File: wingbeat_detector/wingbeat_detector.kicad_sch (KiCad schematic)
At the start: 9 parts, among them J1 USB_C_10137062-00021LF, J2 CONN_UMC_JACK_SMD, U1 UAF42_SMA, U2 MAX865EUA+

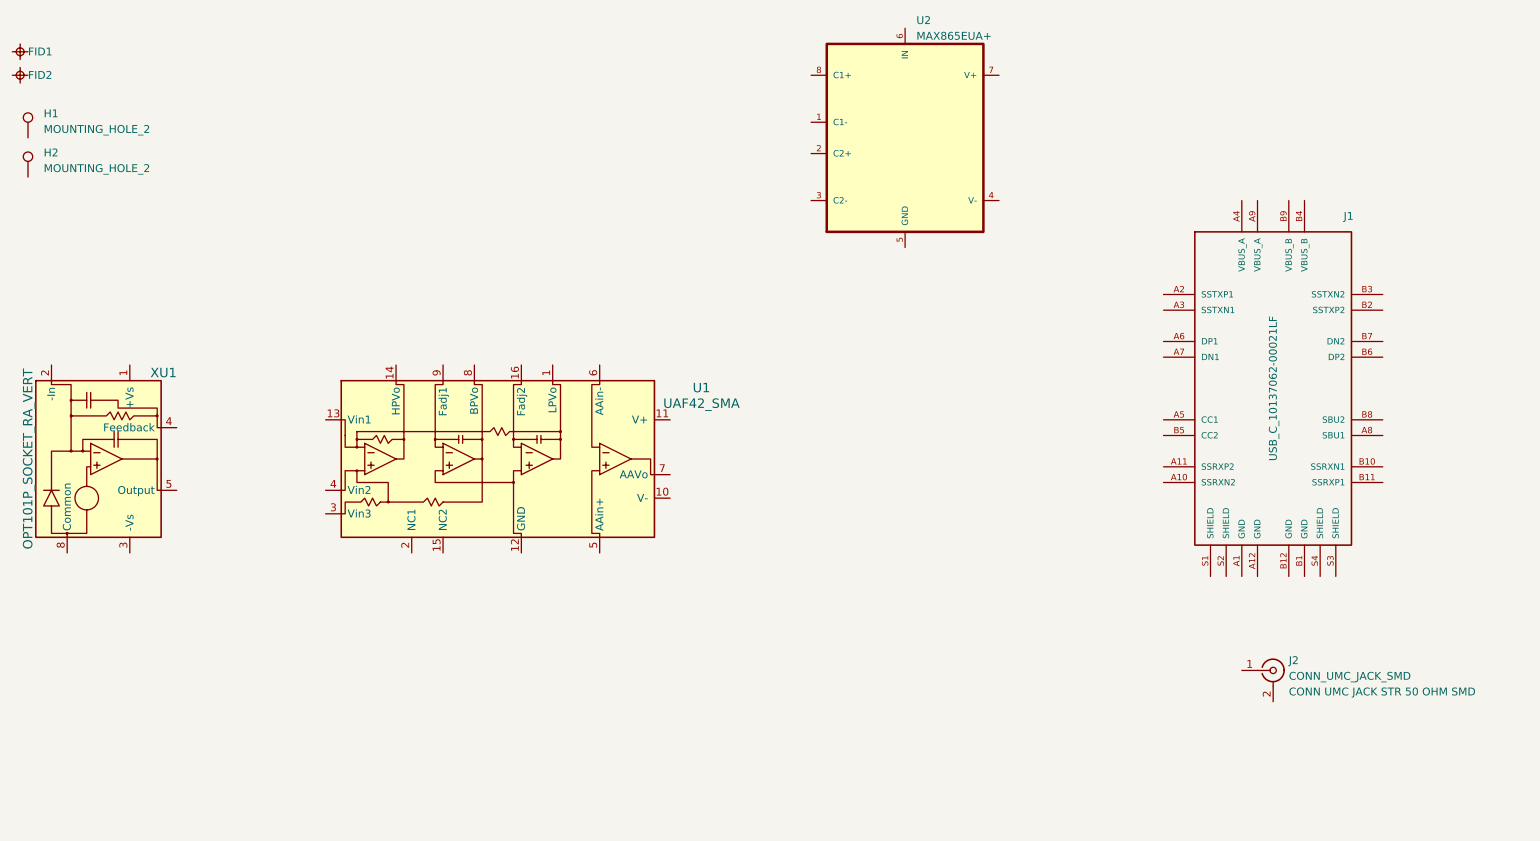
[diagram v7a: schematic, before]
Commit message: Remove OPT101 and replace
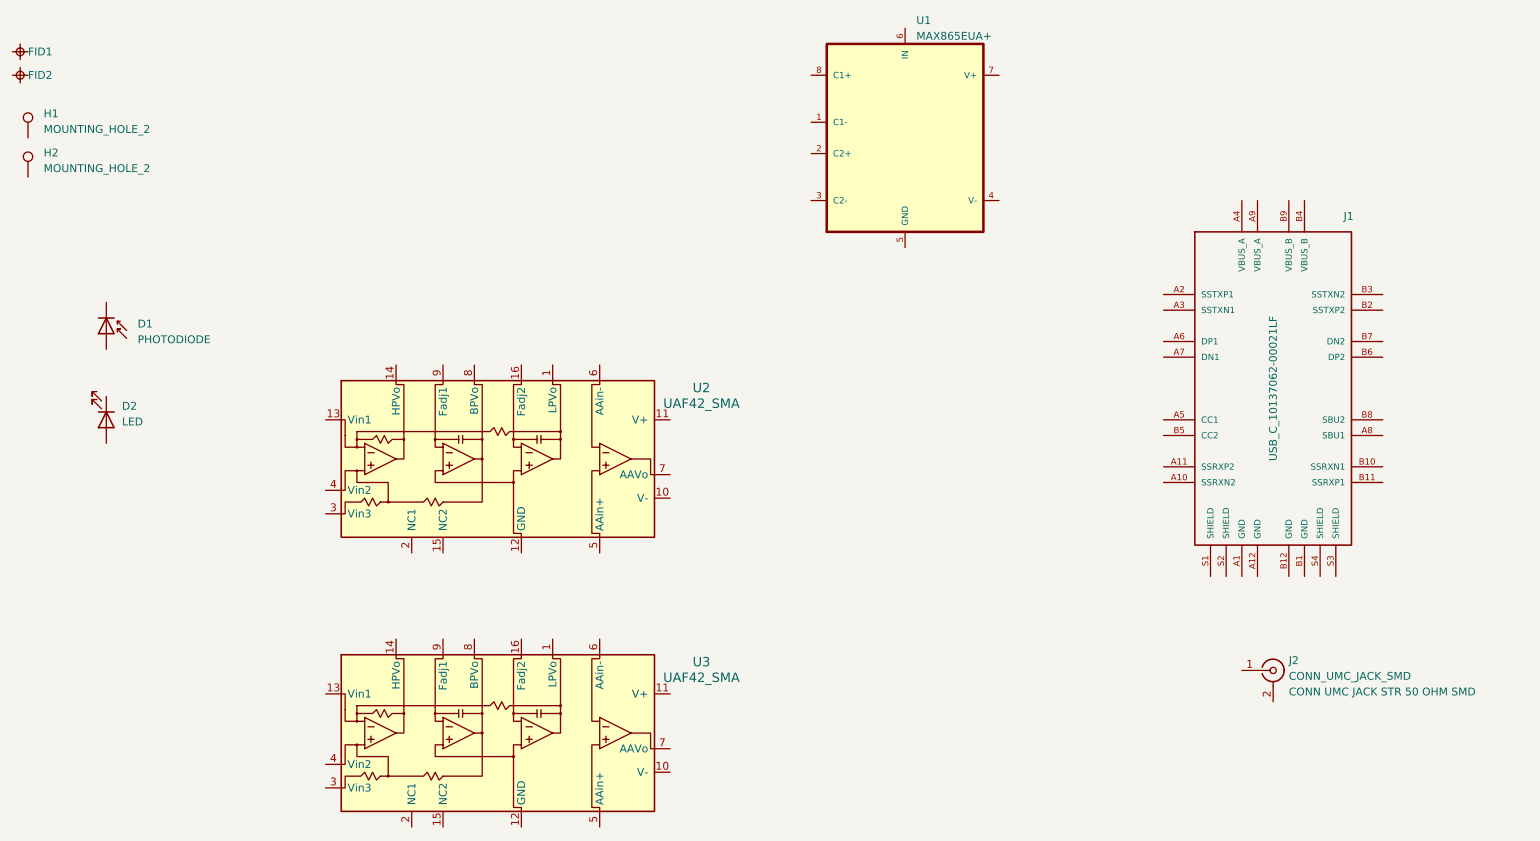
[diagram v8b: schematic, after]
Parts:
- removed XU1: OPT101P_SOCKET_RA_VERT, Janelia:SOCKET_DIP_2x4_RA_VERT, symbol Janelia:OPT101P_SOCKET_RA_VERT
- added D1: PHOTODIODE, Janelia:PHOTODIODE_RADIAL_RA_SMD_BRIGHT, symbol Janelia:PHOTODIODE_940nm_RADIAL_RA_SMD_BRIGHT
- added D2: LED, Janelia:LED_RADIAL_RA_SMD_BRIGHT, symbol Janelia:LED_940nm_RADIAL_RA_SMD_BRIGHT
- added U3: UAF42_SMA, Janelia:SOIC-16W_7.5x10.3mm_P1.27mm, symbol Janelia:UAF42_SMA
- renumbered U2 to U1, U1 to U2
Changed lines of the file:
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@@
   (symbol (lib_id "Janelia:MAX865EUA+") (at 171.45 38.1 0) (unit 1)
     (in_bom yes) (on_board yes) (dnp no) (fields_autoplaced)
-    (property "Reference" "U2" (at 173.2789 19.05 0)
+    (property "Reference" "U1" (at 173.2789 19.05 0)
       (effects (font (size 1.27 1.27)) (justify left))
     )
@@
       (project "wingbeat_detector"
         (path "/cc457ebc-4af6-4663-b19f-8cb38f061cb4"
-          (reference "U2") (unit 1)
+          (reference "U1") (unit 1)
         )
       )
@@
         (path "/cc457ebc-4af6-4663-b19f-8cb38f061cb4"
           (reference "H1") (unit 1)
+        )
+      )
+    )
+  )
+  (symbol (lib_id "Janelia:LED_940nm_RADIAL_RA_SMD_BRIGHT") (at 41.91 83.82 270) (unit 1)
+    (in_bom yes) (on_board yes) (dnp no) (fields_autoplaced)
+    (property "Reference" "D2" (at 44.45 81.5975 90)
+      (effects (font (size 1.27 1.27)) (justify left))
+    )
+    (property "Value" "LED" (at 44.45 84.1375 90)
+      (effects (font (size 1.27 1.27)) (justify left))
+    )
+    (property "Footprint" "Janelia:LED_RADIAL_RA_SMD_BRIGHT" (at 54.61 83.82 0)
+      (effects (font (size 1.27 1.27)) hide)
+    )
+    (property "Datasheet" "~" (at 41.91 83.82 0)
+      (effects (font (size 1.27 1.27)) hide)
+    )
+    (property "Manufacturer" "American Bright Optoelectronics Corporation" (at 57.15 83.82 0)
+      (effects (font (size 1.27 1.27)) hide)
+    )
+    (property "Manufacturer Part Number" "BIR-BM17J8V-FZ04" (at 52.07 83.82 0)
+      (effects (font (size 1.27 1.27)) hide)
+    )
+    (property "Vendor" "Digi-Key" (at 36.83 83.82 0)
+      (effects (font (size 1.27 1.27)) hide)
+    )
+    (property "Vendor Part Number" "BIR-BM17J8V-FZ04CT-ND" (at 46.99 83.82 0)
+      (effects (font (size 1.27 1.27)) hide)
+    )
+    (property "Description" "5MM 940 IR" (at 49.53 83.82 0)
+      (effects (font (size 1.27 1.27)) hide)
+    )
+    (pin "1")
+    (pin "2")
+    (instances
+      (project "wingbeat_detector"
+        (path "/cc457ebc-4af6-4663-b19f-8cb38f061cb4"
+          (reference "D2") (unit 1)
+        )
+      )
+    )
+  )
+  (symbol (lib_id "Janelia:UAF42_SMA") (at 105.41 134.62 0) (unit 1)
+    (in_bom yes) (on_board yes) (dnp no) (fields_autoplaced)
+    (property "Reference" "U3" (at 138.43 123.0883 0)
+      (effects (font (size 1.524 1.524)))
+    )
+    (property "Value" "UAF42_SMA" (at 138.43 125.6283 0)
+      (effects (font (size 1.524 1.524)))
+    )
+    (property "Footprint" "Janelia:SOIC-16W_7.5x10.3mm_P1.27mm" (at 127 123.19 0)
+      (effects (font (size 1.524 1.524)) hide)
+    )
+    (property "Datasheet" "" (at 129.54 120.65 0)
+      (effects (font (size 1.524 1.524)))
+    )
+    (property "Vendor" "Digi-Key" (at 132.08 118.11 0)
+      (effects (font (size 1.524 1.524)) hide)
+    )
+    (property "Vendor Part Number" "UAF42AU-ND" (at 134.62 115.57 0)
+      (effects (font (size 1.524 1.524)) hide)
+    )
+    (property "Description" "IC UNIV ACTIVE FILTER 16-SOIC" (at 137.16 113.03 0)
+      (effects (font (size 1.524 1.524)) hide)
+    )
+    (property "Manufacturer" "Texas Instruments" (at 105.41 134.62 0)
+      (effects (font (size 1.27 1.27)) hide)
+    )
+    (property "Manufacturer Part Number" "UAF42AU" (at 105.41 134.62 0)
+      (effects (font (size 1.27 1.27)) hide)
+    )
+    (pin "1")
+    (pin "10")
+    (pin "11")
+    (pin "12")
+    (pin "13")
+    (pin "14")
+    (pin "15")
+    (pin "16")
+    (pin "2")
+    (pin "3")
+    (pin "4")
+    (pin "5")
+    (pin "6")
+    (pin "7")
+    (pin "8")
+    (pin "9")
+    (instances
+      (project "wingbeat_detector"
+        (path "/cc457ebc-4af6-4663-b19f-8cb38f061cb4"
+          (reference "U3") (unit 1)
         )
       )
@@
     )
   )
+  (symbol (lib_id "Janelia:PHOTODIODE_940nm_RADIAL_RA_SMD_BRIGHT") (at 41.91 69.85 270) (unit 1)
+    (in_bom yes) (on_board yes) (dnp no) (fields_autoplaced)
+    (property "Reference" "D1" (at 46.99 68.2625 90)
+      (effects (font (size 1.27 1.27)) (justify left))
+    )
+    (property "Value" "PHOTODIODE" (at 46.99 70.8025 90)
+      (effects (font (size 1.27 1.27)) (justify left))
+    )
+    (property "Footprint" "Janelia:PHOTODIODE_RADIAL_RA_SMD_BRIGHT" (at 54.61 69.85 0)
+      (effects (font (size 1.27 1.27)) hide)
+    )
+    (property "Datasheet" "~" (at 41.91 68.58 0)
+      (effects (font (size 1.27 1.27)) hide)
+    )
+    (property "Manufacturer" "American Bright Optoelectronics Corporation" (at 57.15 69.85 0)
+      (effects (font (size 1.27 1.27)) hide)
+    )
+    (property "Manufacturer Part Number" "BPD-BQDA38V-FZ04" (at 49.53 69.85 0)
+      (effects (font (size 1.27 1.27)) hide)
+    )
+    (property "Vendor" "Digi-Key" (at 36.83 69.85 0)
+      (effects (font (size 1.27 1.27)) hide)
+    )
+    (property "Vendor Part Number" "BPD-BQDA38V-FZ04CT-ND" (at 46.99 69.85 0)
+      (effects (font (size 1.27 1.27)) hide)
+    )
+    (property "Description" "SENSOR PHOTODIODE RADIAL" (at 52.07 69.85 0)
+      (effects (font (size 1.27 1.27)) hide)
+    )
+    (pin "1")
+    (pin "2")
+    (instances
+      (project "wingbeat_detector"
+        (path "/cc457ebc-4af6-4663-b19f-8cb38f061cb4"
+          (reference "D1") (unit 1)
+        )
+      )
+    )
+  )
   (symbol (lib_id "Janelia:UAF42_SMA") (at 105.41 90.17 0) (unit 1)
     (in_bom yes) (on_board yes) (dnp no) (fields_autoplaced)
-    (property "Reference" "U1" (at 138.43 78.6383 0)
+    (property "Reference" "U2" (at 138.43 78.6383 0)
       (effects (font (size 1.524 1.524)))
     )
@@
       (project "wingbeat_detector"
         (path "/cc457ebc-4af6-4663-b19f-8cb38f061cb4"
-          (reference "U1") (unit 1)
-        )
-      )
-    )
-  )
-  (symbol (lib_id "Janelia:OPT101P_SOCKET_RA_VERT") (at 40.64 90.17 0) (unit 1)
-    (in_bom yes) (on_board yes) (dnp no)
-    (property "Reference" "XU1" (at 53.34 76.2 0)
-      (effects (font (size 1.524 1.524)) (justify right))
-    )
-    (property "Value" "OPT101P_SOCKET_RA_VERT" (at 29.21 90.17 90)
-      (effects (font (size 1.524 1.524)))
-    )
-    (property "Footprint" "Janelia:SOCKET_DIP_2x4_RA_VERT" (at 40.64 57.15 0)
-      (effects (font (size 1.27 1.27)) hide)
-    )
-    (property "Datasheet" "" (at 40.64 90.17 0)
-      (effects (font (size 1.27 1.27)) hide)
-    )
-    (property "Manufacturer" "Aries Electronics" (at 40.64 59.69 0)
-      (effects (font (size 1.27 1.27)) hide)
-    )
-    (property "Manufacturer Part Number" "08-810-90" (at 40.64 64.77 0)
-      (effects (font (size 1.27 1.27)) hide)
-    )
-    (property "Vendor" "Digi-Key" (at 40.64 52.07 0)
-      (effects (font (size 1.27 1.27)) hide)
-    )
-    (property "Vendor Part Number" "A117-ND" (at 40.64 62.23 0)
-      (effects (font (size 1.27 1.27)) hide)
-    )
-    (property "Description" "CONN IC DIP SOCKET 8POS GOLD" (at 40.64 54.61 0)
-      (effects (font (size 1.27 1.27)) hide)
-    )
-    (pin "1")
-    (pin "2")
-    (pin "3")
-    (pin "4")
-    (pin "5")
-    (pin "8")
-    (instances
-      (project "wingbeat_detector"
-        (path "/cc457ebc-4af6-4663-b19f-8cb38f061cb4"
-          (reference "XU1") (unit 1)
-        )
-      )
+          (reference "U2") (unit 1)
+        )
+      )
